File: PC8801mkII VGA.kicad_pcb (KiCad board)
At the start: 2 copper layers, 39.4 x 31.8 mm, 5 parts

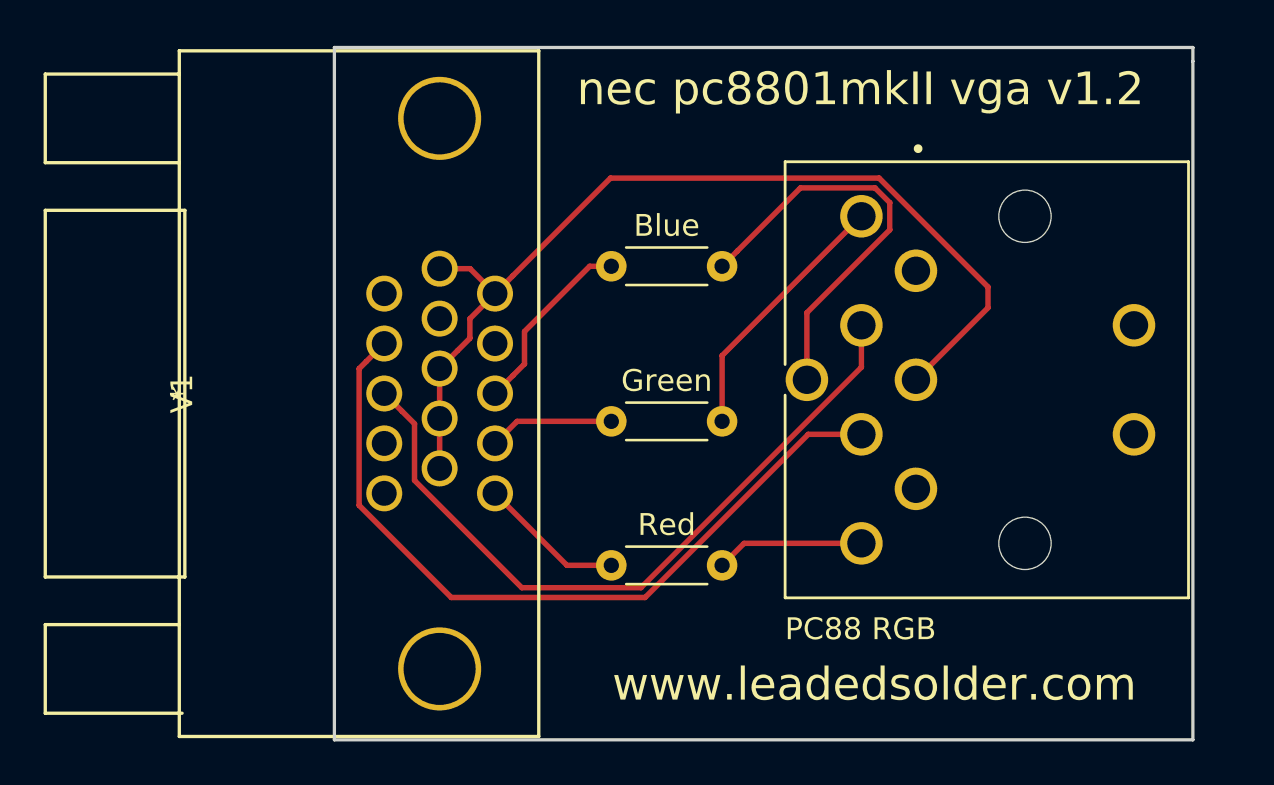
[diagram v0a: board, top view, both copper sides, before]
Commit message: Flipped the connector so it actually lines up now
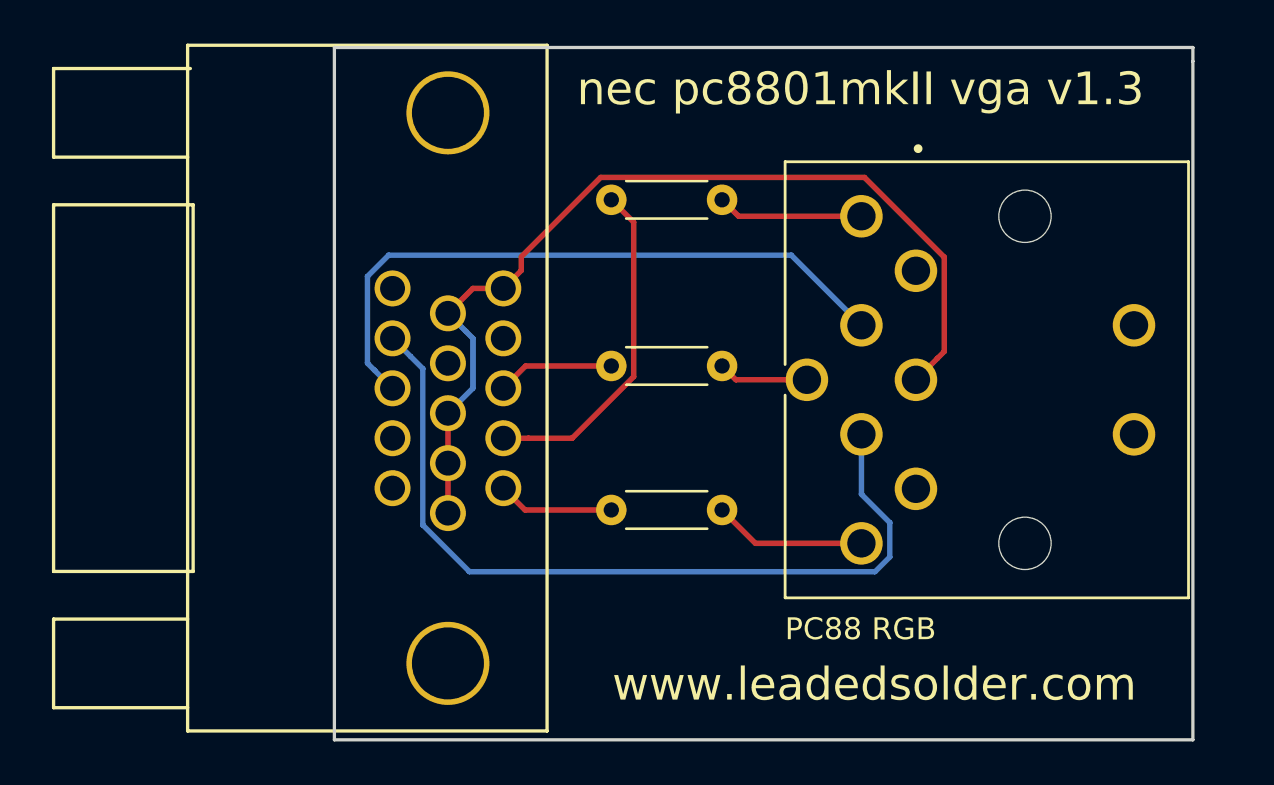
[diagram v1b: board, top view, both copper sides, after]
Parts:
- removed Blue, Green, Red: 150, Resistors_ThroughHole:R_Axial_DIN0204_L3.6mm_D1.6mm_P5.08mm_Horizontal
- added R1: 150, Resistors_ThroughHole:R_Axial_DIN0204_L3.6mm_D1.6mm_P5.08mm_Horizontal, F.Cu at (188.0, 113.3)
- added R2: 150, Resistors_ThroughHole:R_Axial_DIN0204_L3.6mm_D1.6mm_P5.08mm_Horizontal, F.Cu at (188.0, 99.1)
- added R3: 150, Resistors_ThroughHole:R_Axial_DIN0204_L3.6mm_D1.6mm_P5.08mm_Horizontal, F.Cu at (188.0, 106.7)
- moved V1 0.46 mm to (168.7, 107.7)
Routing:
- net /Blue: track 19.2 -> 4.15 mm
- net /Green_VGA: track 5.75 -> 15.7 mm
- net /Green: track 12.1 -> 6.70 mm
- net /Blue_VGA: track 8.62 -> 5.38 mm
- net /V-Sync: track 33.2 -> 30.0 mm
- net /H-Sync: track 35.8 -> 37.9 mm
- net /Red_VGA: track 6.70 -> 5.37 mm
- net /GND: track 44.6 -> 43.5 mm
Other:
- board text added: "1"
- board text added: "15"
- board text added: "Blue"
- board text added: "Green"
- board text added: "Red"
- board text added: "nec pc8801mkII vga v1.3"
- board text removed: "nec pc8801mkII vga v1.2"

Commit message: V1.4 - the colour pins go to the right places now
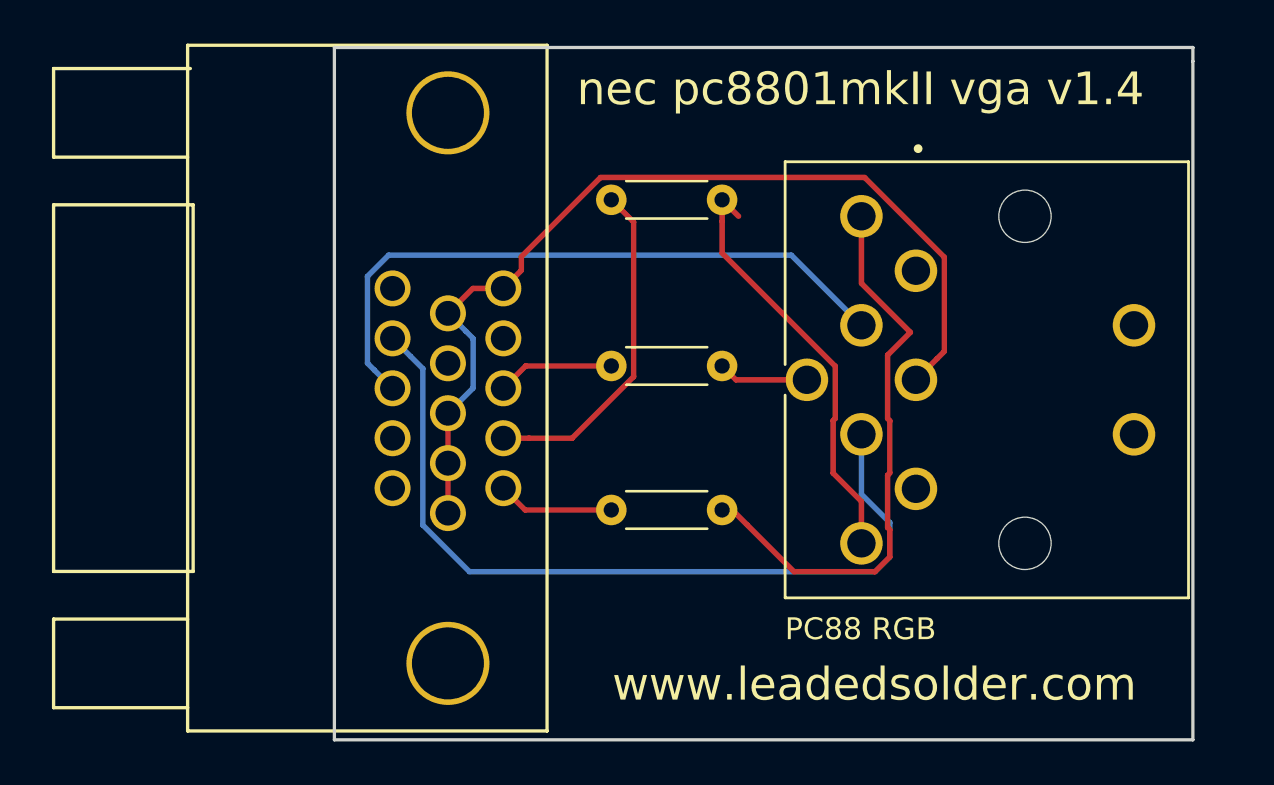
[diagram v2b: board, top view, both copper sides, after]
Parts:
- removed R1, R2: 150, Resistors_ThroughHole:R_Axial_DIN0204_L3.6mm_D1.6mm_P5.08mm_Horizontal
- added RGreen1: 150, Resistors_ThroughHole:R_Axial_DIN0204_L3.6mm_D1.6mm_P5.08mm_Horizontal, F.Cu at (188.0, 99.1)
- added RRed1: 150, Resistors_ThroughHole:R_Axial_DIN0204_L3.6mm_D1.6mm_P5.08mm_Horizontal, F.Cu at (188.0, 113.3)
- R3: value 150 -> RBlue
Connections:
- N1 pad 6: /Green -> /Red
- N1 pad 7: /Red -> /Green
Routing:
- net /Red: track 7.19 -> 25.8 mm
- net /Green: track 6.70 -> 19.7 mm
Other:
- board text added: "nec pc8801mkII vga v1.4"
- board text removed: "nec pc8801mkII vga v1.3"

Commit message: Try to route the green trace a little further away from the sync pins
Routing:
- net /Green: track 19.7 -> 22.5 mm
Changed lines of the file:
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@@
     (thickness 1.6)
     (drawings 14)
-    (tracks 65)
+    (tracks 64)
     (zones 0)
     (modules 5)
@@
   (segment (start 199.43 99.815) (end 199.43 102.890998) (width 0.25) (layer F.Cu) (net 2))
   (segment (start 199.31 114.935) (end 199.43 114.815) (width 0.25) (layer F.Cu) (net 3))
-  (segment (start 193.795 99.815) (end 193.04 99.06) (width 0.25) (layer F.Cu) (net 3))
-  (segment (start 193.04 100.049949) (end 193.04 99.06) (width 0.25) (layer F.Cu) (net 3))
-  (segment (start 198.230001 106.690999) (end 193.04 101.500998) (width 0.25) (layer F.Cu) (net 3))
-  (segment (start 193.04 101.500998) (end 193.04 100.049949) (width 0.25) (layer F.Cu) (net 3))
-  (segment (start 198.230001 109.090997) (end 198.230001 106.690999) (width 0.25) (layer F.Cu) (net 3))
-  (segment (start 198.129999 109.190999) (end 198.230001 109.090997) (width 0.25) (layer F.Cu) (net 3))
-  (segment (start 198.129999 111.590997) (end 198.129999 109.190999) (width 0.25) (layer F.Cu) (net 3))
-  (segment (start 199.43 112.890998) (end 198.129999 111.590997) (width 0.25) (layer F.Cu) (net 3))
-  (segment (start 199.43 114.815) (end 199.43 112.890998) (width 0.25) (layer F.Cu) (net 3))
+  (segment (start 196.596 99.06) (end 193.04 99.06) (width 0.25) (layer F.Cu) (net 3))
+  (segment (start 197.104 99.568) (end 196.596 99.06) (width 0.25) (layer F.Cu) (net 3))
+  (segment (start 199.136 107.762) (end 199.136 107.188) (width 0.25) (layer F.Cu) (net 3))
+  (segment (start 197.104 105.156) (end 197.104 99.568) (width 0.25) (layer F.Cu) (net 3))
+  (segment (start 199.136 107.188) (end 197.104 105.156) (width 0.25) (layer F.Cu) (net 3))
+  (segment (start 196.883 110.015) (end 199.136 107.762) (width 0.25) (layer F.Cu) (net 3))
+  (segment (start 196.883 112.268) (end 196.883 110.015) (width 0.25) (layer F.Cu) (net 3))
+  (segment (start 199.43 114.815) (end 196.883 112.268) (width 0.25) (layer F.Cu) (net 3))
   (segment (start 178.752499 106.239499) (end 177.927 105.414) (width 0.25) (layer B.Cu) (net 4))
   (segment (start 179.316499 106.803499) (end 178.752499 106.239499) (width 0.25) (layer B.Cu) (net 4))

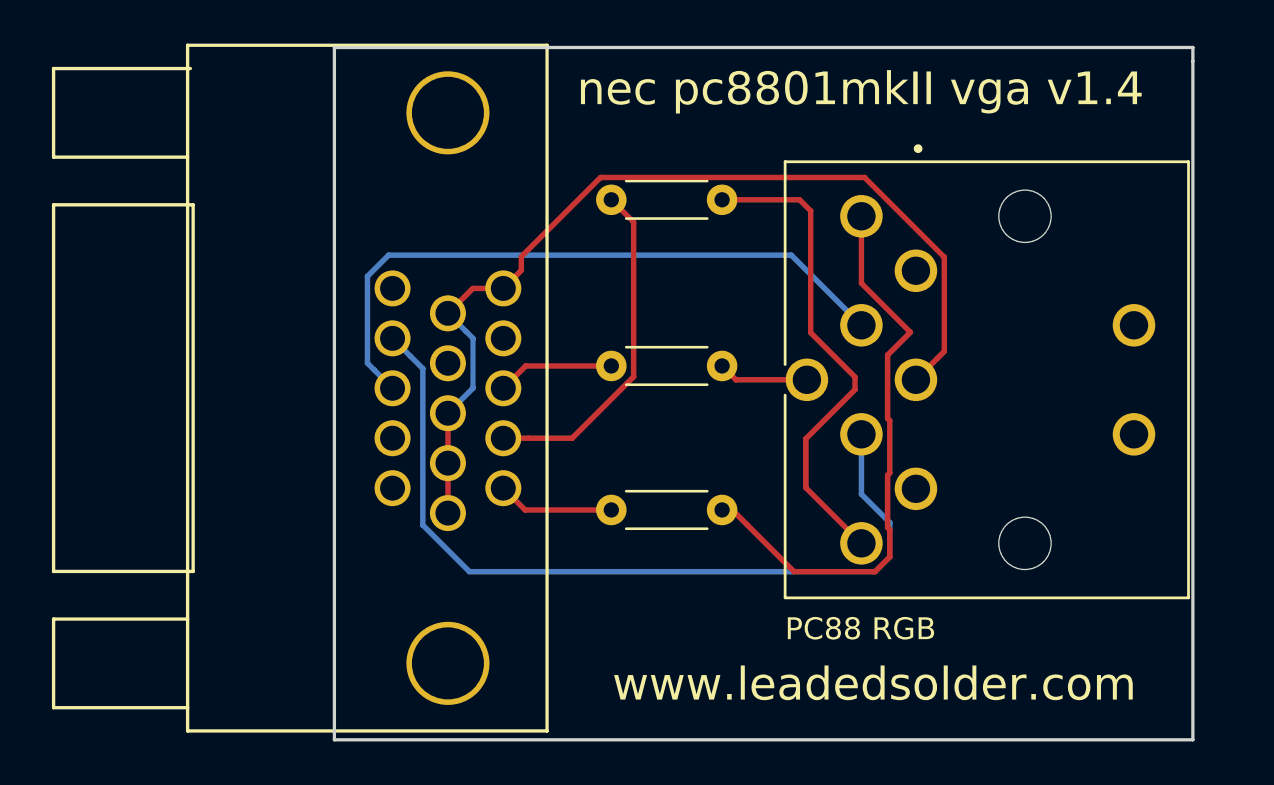
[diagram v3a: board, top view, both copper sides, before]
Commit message: Bigger resistors, trying to shorten colour tracks, run sync far away from all colours
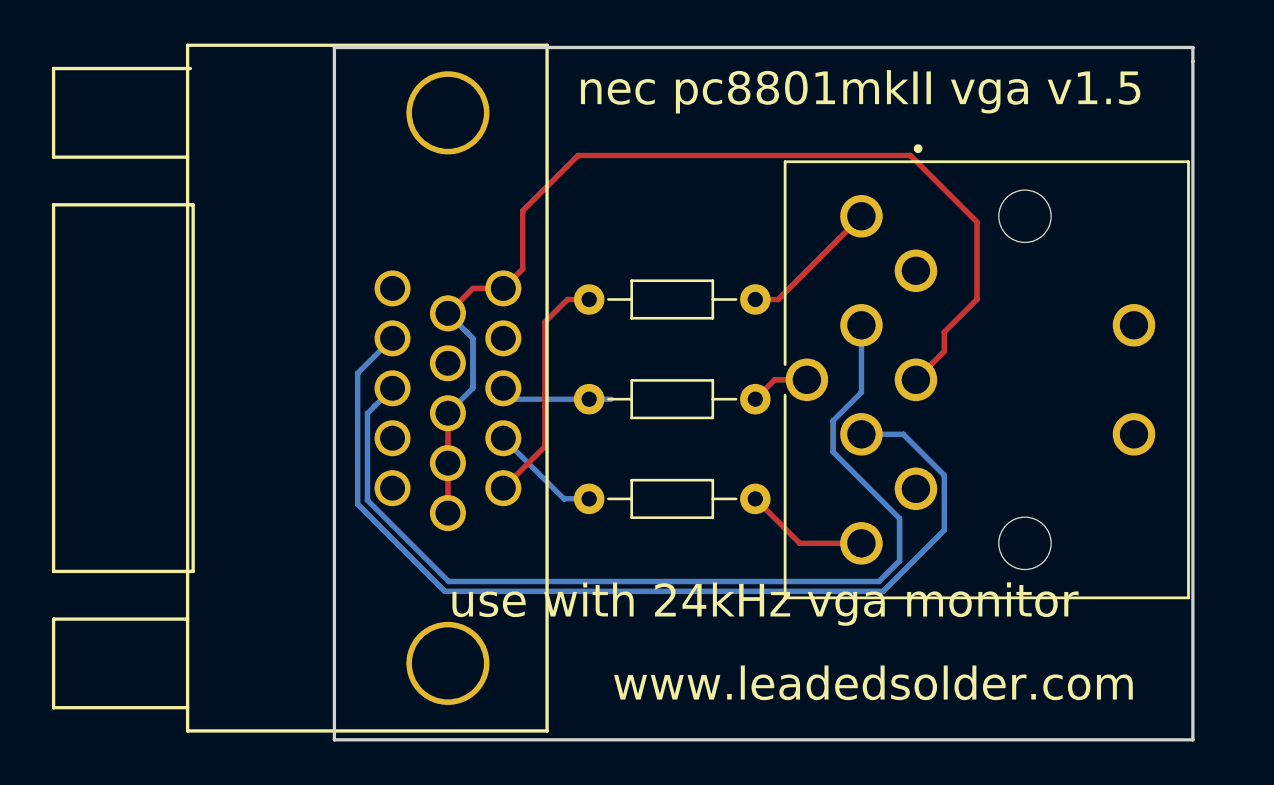
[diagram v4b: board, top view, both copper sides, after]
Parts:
- R3, RGreen1, RRed1: footprint Resistors_ThroughHole:R_Axial_DIN0204_L3.6mm_D1.6mm_P5.08mm_Horizontal -> Resistors_ThroughHole:R_Axial_DIN0204_L3.6mm_D1.6mm_P7.62mm_Horizontal
- moved RGreen1 13.8 mm to (186.9, 112.8)
- moved RRed1 9.71 mm to (186.9, 103.6)
- moved R3 1.83 mm to (186.9, 108.2)
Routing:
- net /Red: track 25.8 -> 6.45 mm
- net /Green: track 22.5 -> 5.88 mm
- net /V-Sync: track 30.0 -> 44.6 mm
- net /Green_VGA: track 15.7 -> 5.09 mm
- net /H-Sync: track 37.9 -> 45.1 mm
- net /Red_VGA: track 5.37 -> 10.9 mm
- net /GND: track 43.5 -> 48.6 mm
- net /Blue: track 4.15 -> 2.73 mm
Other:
- board text added: "nec pc8801mkII vga v1.5"
- board text added: "use with 24kHz vga monitor"
- board text removed: "nec pc8801mkII vga v1.4"
- board text removed: "use with 15/24kHz vga monitor"

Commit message: Ground plane
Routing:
- added copper zone on B.Cu, net /GND
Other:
- board text added: "nec pc8801mkII vga v1.6"
- board text removed: "nec pc8801mkII vga v1.5"
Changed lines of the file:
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@@
-(kicad_pcb (version 20171130) (host pcbnew "(5.0.0-3-g5ebb6b6)")
+(kicad_pcb (version 20171130) (host pcbnew "(5.1.4-0-10_14)")
   (general
     (thickness 1.6)
@@
     (zone_45_only no)
     (trace_min 0.2)
-    (segment_width 0.2)
-    (edge_width 0.15)
     (via_size 0.8)
     (via_drill 0.4)
@@
     (uvia_min_size 0.2)
     (uvia_min_drill 0.1)
+    (edge_width 0.15)
+    (segment_width 0.2)
     (pcb_text_width 0.3)
     (pcb_text_size 1.5 1.5)
@@
     (effects (font (size 1.5 1.5) (thickness 0.3)) (justify mirror))
   )
-  (gr_text "nec pc8801mkII vga v1.5" (at 199.39 93.98) (layer F.SilkS)
+  (gr_text "nec pc8801mkII vga v1.6" (at 199.39 93.98) (layer F.SilkS)
     (effects (font (size 1.5 1.5) (thickness 0.3)))
   )
@@
   (segment (start 183.506872 108.204) (end 183.007 107.704128) (width 0.25) (layer B.Cu) (net 10))
   (segment (start 187.96 108.204) (end 183.506872 108.204) (width 0.25) (layer B.Cu) (net 10))
+  (zone (net 7) (net_name /GND) (layer B.Cu) (hatch edge 0.508)
+    (connect_pads (clearance 0.508))
+    (min_thickness 0.254)
+    (fill yes (arc_segments 32) (thermal_gap 0.508) (thermal_bridge_width 0.508))
+    (polygon
+      (pts
+        (xy 214.376 92.456) (xy 214.376 123.444) (xy 175.768 123.444) (xy 175.768 92.456)
+      )
+    )
+  )
 )

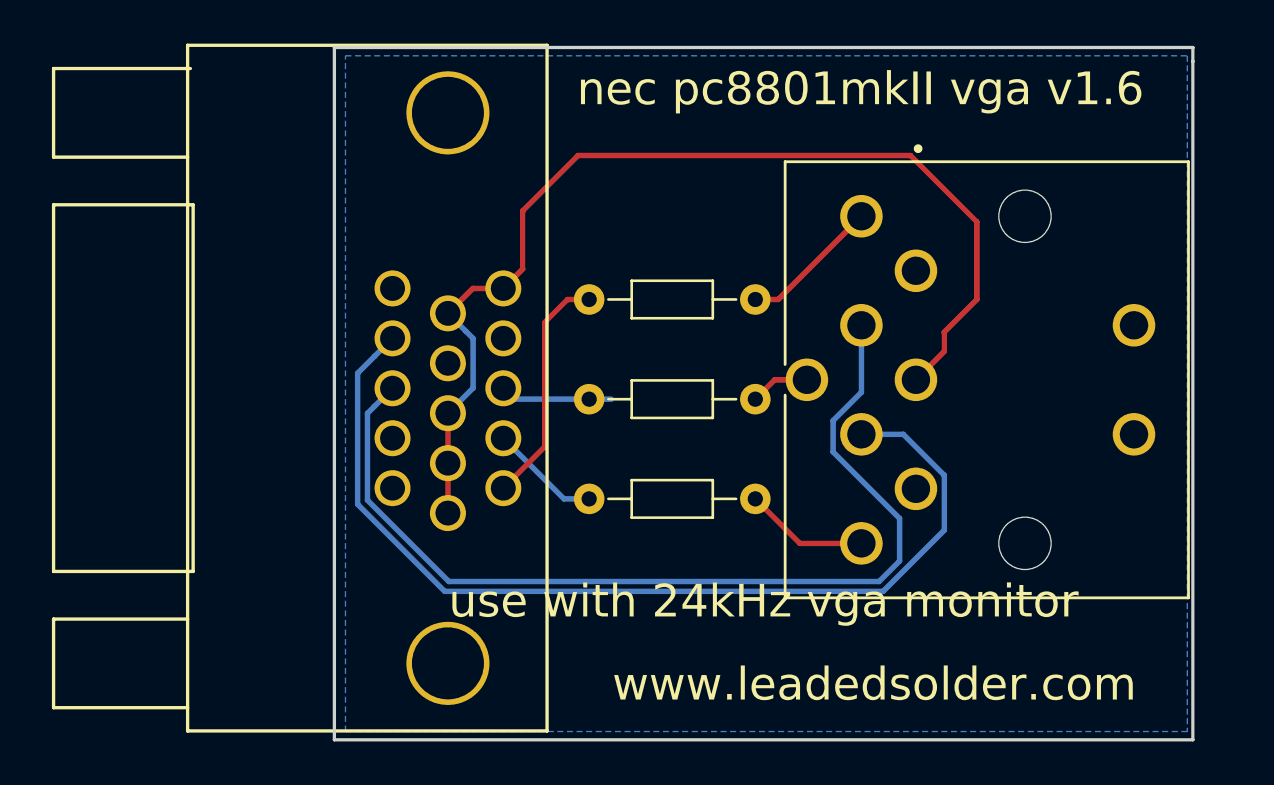
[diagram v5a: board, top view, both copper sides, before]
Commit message: Use decoupling caps
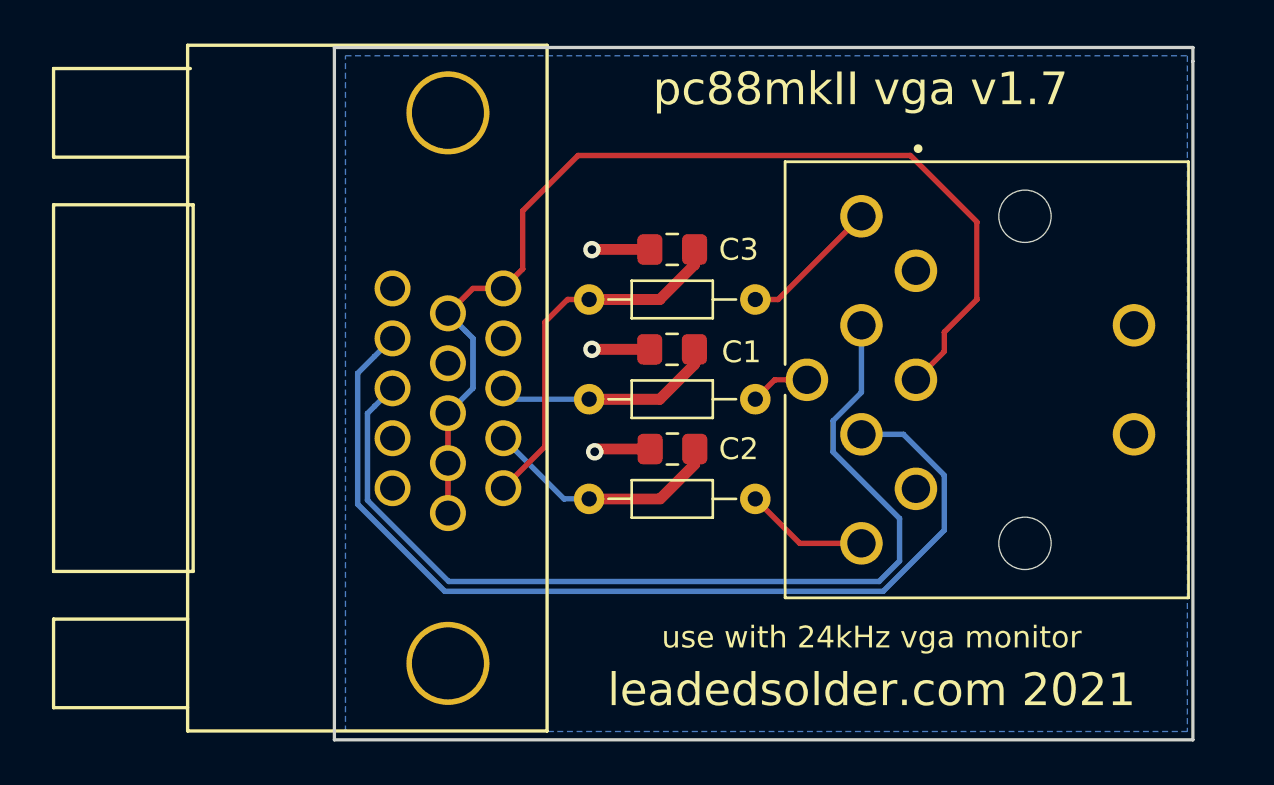
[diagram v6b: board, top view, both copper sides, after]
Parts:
- added C1: 0.1µF, Capacitor_SMD:C_0805_2012Metric_Pad1.15x1.40mm_HandSolder, F.Cu at (190.7, 105.9)
- added C2: 0.1µF, Capacitor_SMD:C_0805_2012Metric_Pad1.15x1.40mm_HandSolder, F.Cu at (190.8, 110.5)
- added C3: 0.1µF, Capacitor_SMD:C_0805_2012Metric_Pad1.15x1.40mm_HandSolder, F.Cu at (190.8, 101.3)
- RBlue1: renamed from R3; value RBlue -> 150Ω
- RGreen1, RRed1: value 150 -> 150Ω
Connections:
- N1 pad 1: /12V -> Net-(N1-Pad1)
- N1 pad 3: /NC -> /12V
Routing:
- net /GND: track 48.6 -> 56.5 mm, vias 0 -> 3
- net /Green_VGA: track 5.09 -> 11.3 mm
- net /Red_VGA: track 10.9 -> 17.1 mm
- net /Blue_VGA: track 5.16 -> 11.3 mm
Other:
- board text added: "leadedsolder.com 2021"
- board text added: "pc88mkII vga v1.7"
- board text removed: "nec pc8801mkII vga v1.6"
- board text removed: "www.leadedsolder.com"
